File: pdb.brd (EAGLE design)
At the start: 85 x 50 mm, 35 parts, among them Q1 20MHz, Q2 IRFR5305PBF, Q3 IRFR5305PBF, U1 TSR_1-2433, U2 LTC2946CMSPBF, U3 LTC2946CMSPBF, U4 LTC2946CMSPBF, U5 ATMEGA48-20AU, U6 TXB0104

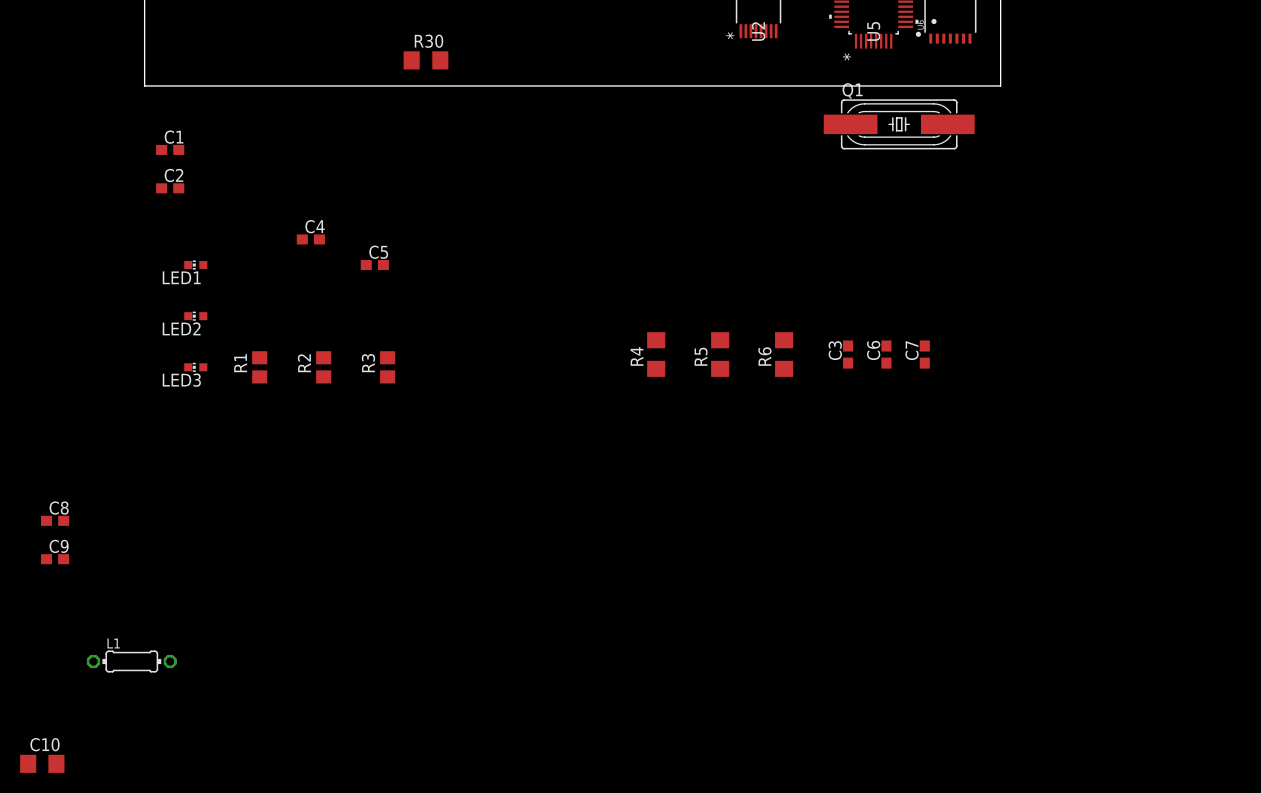
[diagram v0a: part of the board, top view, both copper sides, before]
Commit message: Connected Levelshifter
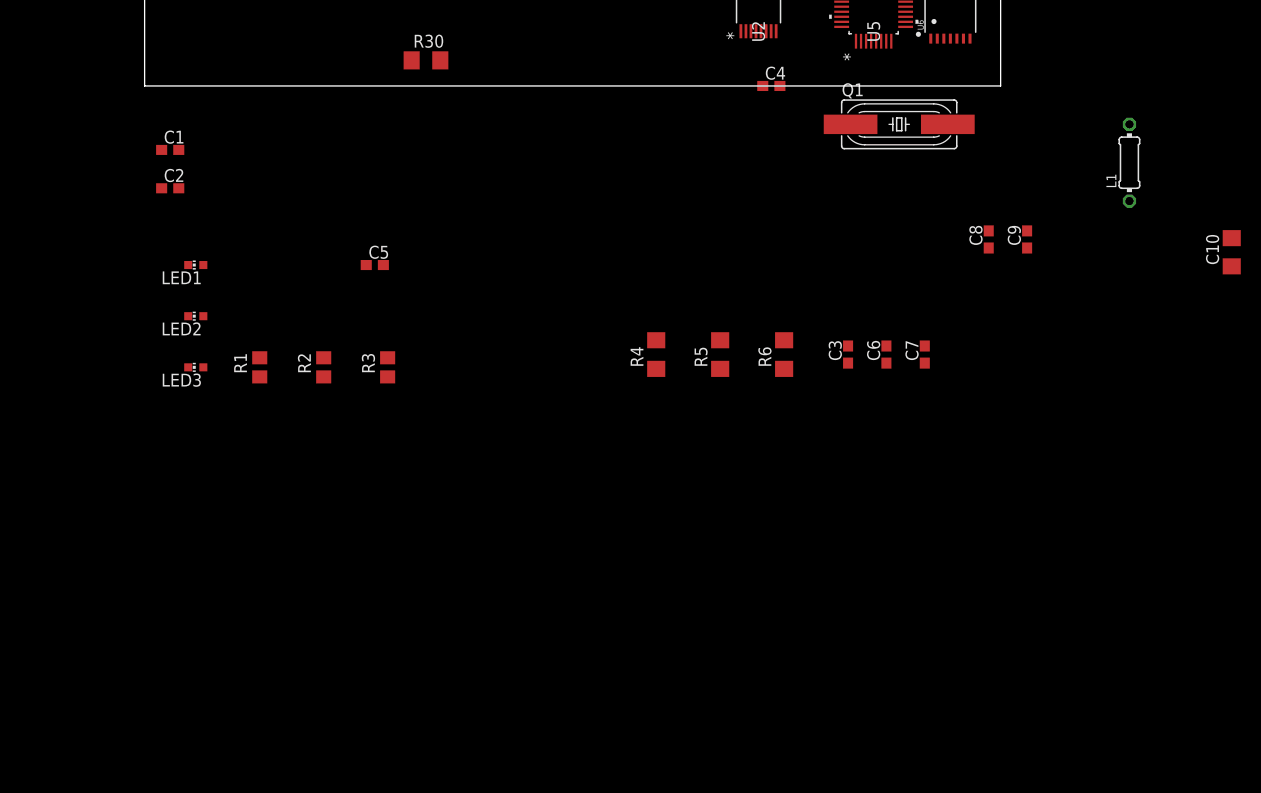
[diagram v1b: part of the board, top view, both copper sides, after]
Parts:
- moved C10 128.6 mm to (108.0, -16.5), turned to 90 degrees
- moved L1 110.8 mm to (97.8, -7.62), turned to 90 degrees
- moved C9 101.6 mm to (87.6, -15.2), turned to 90 degrees
- moved C8 96.8 mm to (83.8, -15.2), turned to 90 degrees
- moved C4 48.2 mm to (62.2, 0.00)
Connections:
- removed net N$24: U5.14
- new net MISO_3V3: U6.2
- new net MOSI_3V3: U6.3
- new net SS_3V3: U6.5
- new net SS_5V: U5.14, U6.10
- net +3V3: now also U6.1
- net +5V: now also U6.14
- net GND: now also U6.7
- net MISO_5V: now also U6.13
- net MOSI_5V: now also U6.12
- net SCK_5V: now also U6.11, U6.4

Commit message: First parts placed
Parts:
- added ESC: XT60PWFEMALE, amass:XT60PWFEMALE
- added JP1: (no value), pinhead:2X08
- moved R4 91.6 mm to (24.1, 61.0), turned to 180 degrees
- moved U5 74.3 mm to (10.2, 48.3)
- moved U4 71.5 mm to (12.7, 38.1)
- moved U$2 70.6 mm to (39.4, 82.5), turned to 0 degrees
- moved U3 70.3 mm to (5.08, 38.1)
- moved U2 60.7 mm to (24.1, 55.9)
- moved R32 58.3 mm to (27.9, 68.6), turned to 270 degrees
- moved R30 54.3 mm to (43.2, 54.6)
- moved D4 47.0 mm to (43.2, 58.4)
- moved Q3 44.9 mm to (34.3, 67.3)
- moved Q2 44.0 mm to (43.2, 67.3)
- moved L3 40.3 mm to (78.7, 15.2)
- moved U1 39.5 mm to (77.5, 20.3)
- moved U$1 30.5 mm to (48.3, 27.9), turned to 180 degrees
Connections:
- net GND: now also ESC.NEG
- net V+: now also ESC.POS
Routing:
- added copper zone on layer 16, net GND
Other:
- board size 85 x 50 mm -> 50 x 85 mm

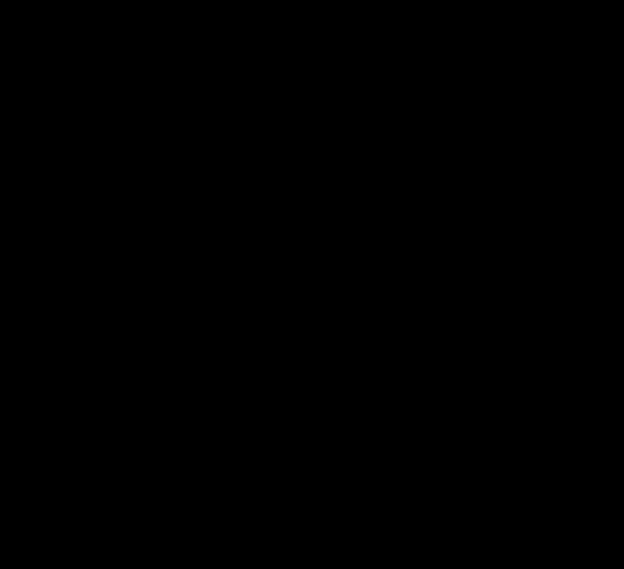
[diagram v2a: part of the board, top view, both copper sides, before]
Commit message: added temperature sensor
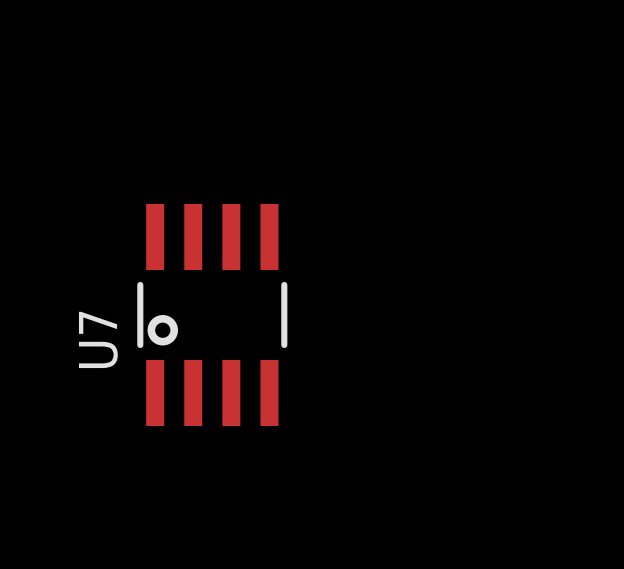
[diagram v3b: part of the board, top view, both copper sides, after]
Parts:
- added U7: AT30TS74SS8M, jonas_microchip:SO08
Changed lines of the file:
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@@
 <element name="ESC" library="amass" package="XT60PWFEMALE" value="XT60PWFEMALE" x="10.16" y="82.55"/>
 <element name="JP1" library="pinhead" library_urn="urn:adsk.eagle:library:325" package="2X08" package3d_urn="urn:adsk.eagle:package:22481/2" value="" x="14.245" y="13.335" rot="R180"/>
+<element name="U7" library="jonas_microchip" library_urn="urn:adsk.eagle:library:891228" package="SO08" package3d_urn="urn:adsk.eagle:package:1422804/3" value="AT30TS74SS8M" x="-21.59" y="-24.13"/>
 </elements>
 <signals>

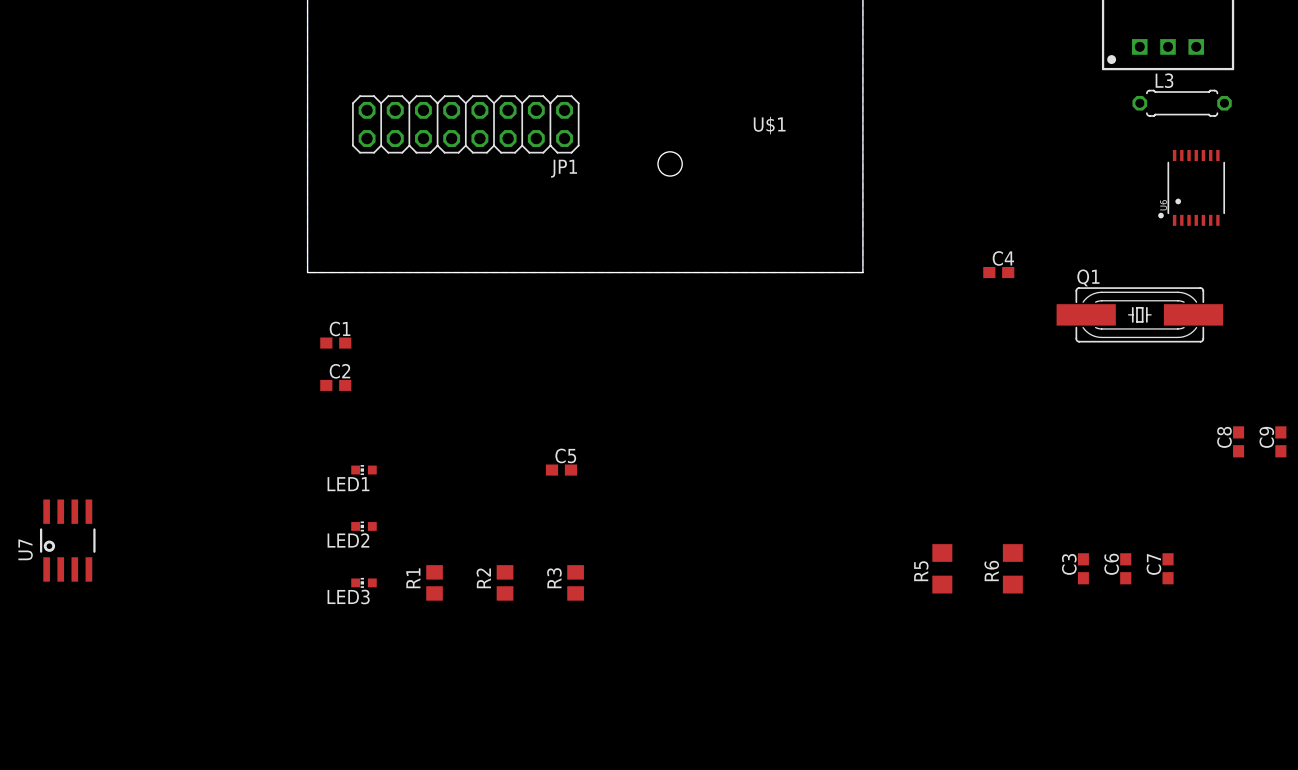
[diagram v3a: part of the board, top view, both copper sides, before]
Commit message: updated inductor for 3v regulator
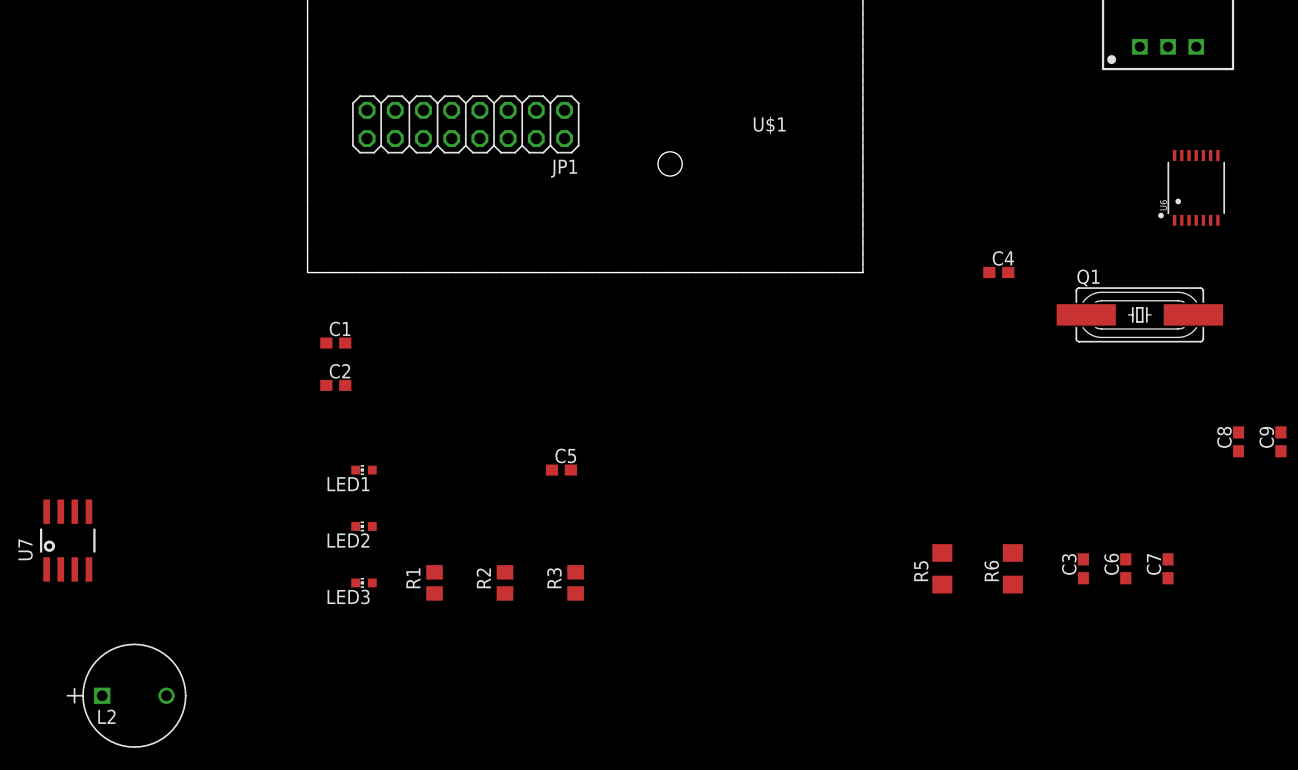
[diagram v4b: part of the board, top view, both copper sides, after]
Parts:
- removed L3: 220µH, resistor:0207/7
- added L2: RLB9012-221KL, jonas_bourns:IND_BOURNS_RLB9012
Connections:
- net N$6: now also L2.2; no longer L3.2
- net SENSE+3V3: now also L2.1; no longer L3.1
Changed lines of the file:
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@@
 <attribute name="SPICEPREFIX" value="C" x="2.54" y="-10.16" size="1.778" layer="27" display="off"/>
 </element>
-<element name="L3" library="resistor" package="0207/7" value="220µH" x="78.74" y="15.24"/>
 <element name="C4" library="resistor" package="C0603" value="100nF" x="62.23" y="0"/>
 <element name="C5" library="resistor" package="C0603" value="100nF" x="22.86" y="-17.78"/>
@@
 <element name="JP1" library="pinhead" library_urn="urn:adsk.eagle:library:325" package="2X08" package3d_urn="urn:adsk.eagle:package:22481/2" value="" x="14.245" y="13.335" rot="R180"/>
 <element name="U7" library="jonas_microchip" library_urn="urn:adsk.eagle:library:891228" package="SO08" package3d_urn="urn:adsk.eagle:package:1422804/3" value="AT30TS74SS8M" x="-21.59" y="-24.13"/>
+<element name="L2" library="jonas_bourns" library_urn="urn:adsk.eagle:library:1422904" package="IND_BOURNS_RLB9012" package3d_urn="urn:adsk.eagle:package:1422907/3" value="RLB9012-221KL" x="-12.7" y="-38.1">
+<attribute name="MANUFACTURER_PART_NUMBER" value="RLB9012221KL" x="-12.7" y="-38.1" size="1.778" layer="27" display="off"/>
+<attribute name="VENDOR" value="Bourns Electronics" x="-12.7" y="-38.1" size="1.778" layer="27" display="off"/>
+</element>
 </elements>
 <signals>
@@
 </signal>
 <signal name="N$6">
-<contactref element="L3" pad="2"/>
 <contactref element="C5" pad="2"/>
 <contactref element="U1" pad="3"/>
-<wire x1="82.55" y1="15.24" x2="80.01" y2="20.32" width="0" layer="19" extent="1-1"/>
-<wire x1="23.71" y1="-17.78" x2="82.55" y2="15.24" width="0" layer="19" extent="1-1"/>
+<contactref element="L2" pad="2"/>
+<wire x1="23.71" y1="-17.78" x2="80.01" y2="20.32" width="0" layer="19" extent="1-1"/>
+<wire x1="-12.7" y1="-38.1" x2="23.71" y2="-17.78" width="0" layer="19" extent="1-1"/>
 </signal>
 <signal name="+3V3">
@@
 <contactref element="C4" pad="1"/>
 <contactref element="R6" pad="1"/>
-<contactref element="L3" pad="1"/>
 <contactref element="U4" pad="16"/>
-<wire x1="61.38" y1="0" x2="74.93" y2="15.24" width="0" layer="19" extent="1-1"/>
+<contactref element="L2" pad="1"/>
 <wire x1="63.5" y1="-28.092" x2="61.38" y2="0" width="0" layer="19" extent="1-1"/>
 <wire x1="10.94866875" y1="40.2844" x2="61.38" y2="0" width="0" layer="19" extent="1-1"/>
+<wire x1="-18.4912" y1="-38.1" x2="63.5" y2="-28.092" width="0" layer="19" extent="1-1"/>
 </signal>
 <signal name="SDA">
